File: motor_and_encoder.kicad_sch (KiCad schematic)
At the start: 6 parts, among them J5_1 Conn_02x03_Odd_Even, J5_2 Conn_02x03_Odd_Even, U5_1 DRV8835DSSR

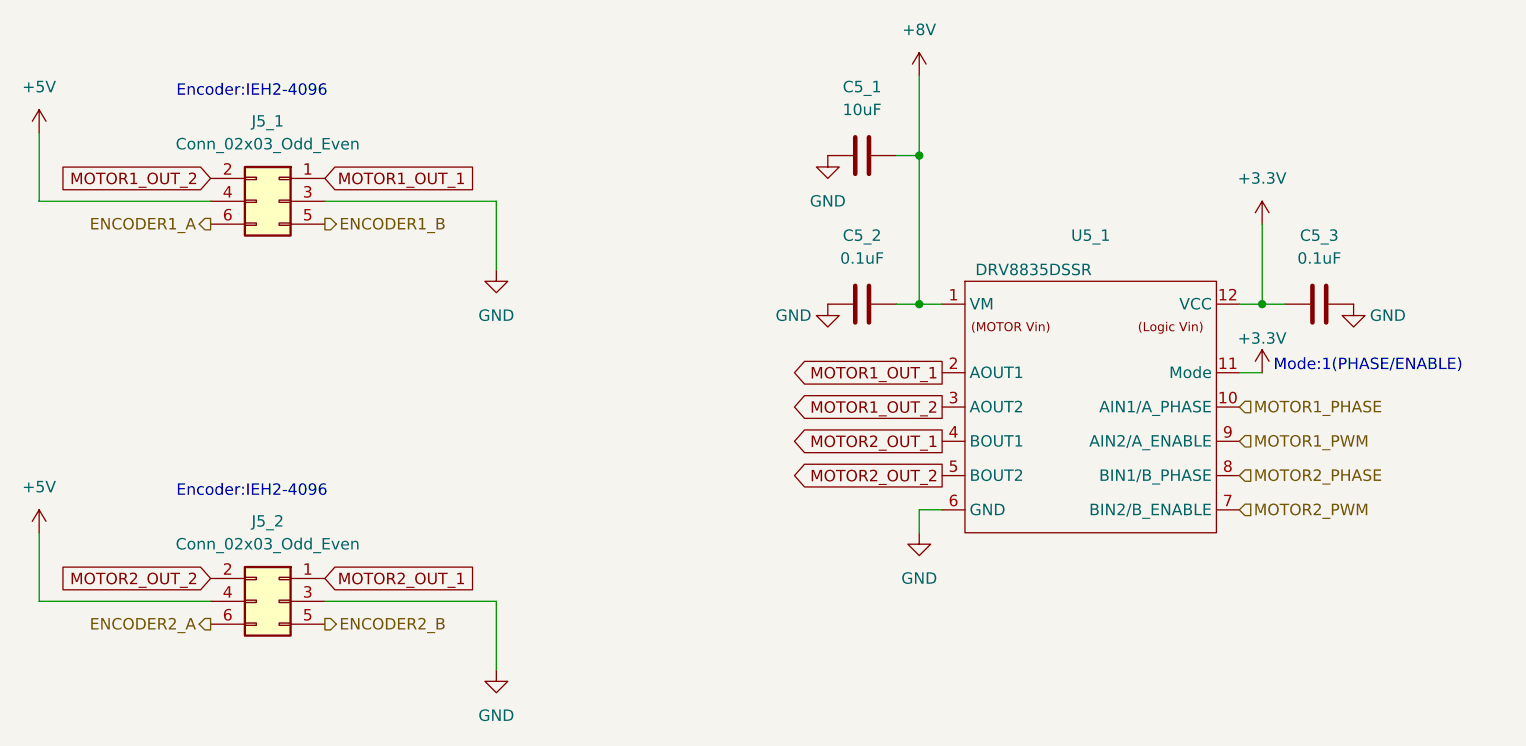
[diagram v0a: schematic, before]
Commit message: シンボルのモータの左右を入れ替え
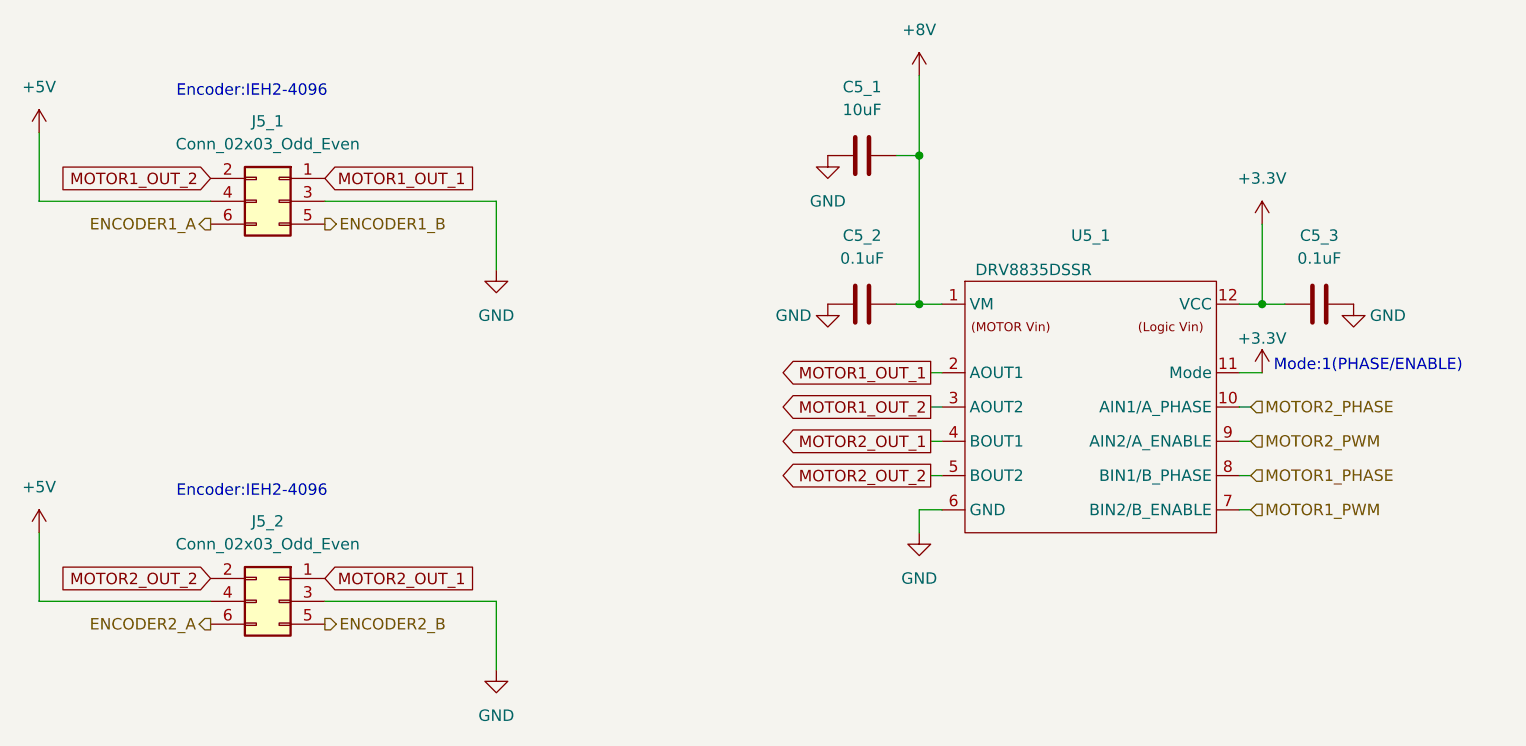
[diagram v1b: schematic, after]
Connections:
- net MOTOR1_PHASE: now also U5_1.8 (BIN1/B_PHASE); no longer U5_1.10 (AIN1/A_PHASE)
- net MOTOR1_PWM: now also U5_1.7 (BIN2/B_ENABLE); no longer U5_1.9 (AIN2/A_ENABLE)
- net MOTOR2_PHASE: now also U5_1.10 (AIN1/A_PHASE); no longer U5_1.8 (BIN1/B_PHASE)
- net MOTOR2_PWM: now also U5_1.9 (AIN2/A_ENABLE); no longer U5_1.7 (BIN2/B_ENABLE)
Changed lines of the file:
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@@
+    (stroke (width 0) (type default))
+  )
+  (wire (pts (xy 191.77 102.87) (xy 193.04 102.87))
     (stroke (width 0) (type default))
   )
   (wire (pts (xy 156.21 58.42) (xy 156.21 67.31))
+    (stroke (width 0) (type default))
+  )
+  (wire (pts (xy 191.77 95.25) (xy 193.04 95.25))
     (stroke (width 0) (type default))
   )
@@
     (stroke (width 0) (type default))
   )
+  (wire (pts (xy 157.48 95.25) (xy 158.75 95.25))
+    (stroke (width 0) (type default))
+  )
   (wire (pts (xy 109.22 72.39) (xy 90.17 72.39))
     (stroke (width 0) (type default))
   )
   (wire (pts (xy 153.67 83.82) (xy 156.21 83.82))
+    (stroke (width 0) (type default))
+  )
+  (wire (pts (xy 157.48 91.44) (xy 158.75 91.44))
     (stroke (width 0) (type default))
   )
@@
     (stroke (width 0) (type default))
   )
+  (wire (pts (xy 157.48 102.87) (xy 158.75 102.87))
+    (stroke (width 0) (type default))
+  )
+  (wire (pts (xy 191.77 106.68) (xy 193.04 106.68))
+    (stroke (width 0) (type default))
+  )
   (wire (pts (xy 109.22 72.39) (xy 109.22 80.01))
     (stroke (width 0) (type default))
   )
   (wire (pts (xy 109.22 116.84) (xy 109.22 124.46))
+    (stroke (width 0) (type default))
+  )
+  (wire (pts (xy 191.77 99.06) (xy 193.04 99.06))
+    (stroke (width 0) (type default))
+  )
+  (wire (pts (xy 157.48 99.06) (xy 158.75 99.06))
     (stroke (width 0) (type default))
   )
@@
     (effects (font (size 1.27 1.27)) (justify left bottom))
   )
-  (global_label "MOTOR1_OUT_2" (shape output) (at 158.75 95.25 180) (fields_autoplaced)
+  (global_label "MOTOR1_OUT_2" (shape output) (at 157.48 95.25 180) (fields_autoplaced)
     (effects (font (size 1.27 1.27)) (justify right))
-    (property "Intersheetrefs" "${INTERSHEET_REFS}" (at 141.432 95.25 0)
+    (property "Intersheetrefs" "${INTERSHEET_REFS}" (at 140.162 95.25 0)
       (effects (font (size 1.27 1.27)) (justify right) hide)
     )
   )
-  (global_label "MOTOR2_OUT_2" (shape output) (at 158.75 102.87 180) (fields_autoplaced)
+  (global_label "MOTOR2_OUT_2" (shape output) (at 157.48 102.87 180) (fields_autoplaced)
     (effects (font (size 1.27 1.27)) (justify right))
-    (property "Intersheetrefs" "${INTERSHEET_REFS}" (at 141.432 102.87 0)
+    (property "Intersheetrefs" "${INTERSHEET_REFS}" (at 140.162 102.87 0)
       (effects (font (size 1.27 1.27)) (justify right) hide)
     )
   )
-  (global_label "MOTOR1_OUT_1" (shape output) (at 158.75 91.44 180) (fields_autoplaced)
+  (global_label "MOTOR1_OUT_1" (shape output) (at 157.48 91.44 180) (fields_autoplaced)
     (effects (font (size 1.27 1.27)) (justify right))
-    (property "Intersheetrefs" "${INTERSHEET_REFS}" (at 141.432 91.44 0)
+    (property "Intersheetrefs" "${INTERSHEET_REFS}" (at 140.162 91.44 0)
       (effects (font (size 1.27 1.27)) (justify right) hide)
     )
   )
-  (global_label "MOTOR2_OUT_1" (shape output) (at 158.75 99.06 180) (fields_autoplaced)
+  (global_label "MOTOR2_OUT_1" (shape output) (at 157.48 99.06 180) (fields_autoplaced)
     (effects (font (size 1.27 1.27)) (justify right))
-    (property "Intersheetrefs" "${INTERSHEET_REFS}" (at 141.432 99.06 0)
+    (property "Intersheetrefs" "${INTERSHEET_REFS}" (at 140.162 99.06 0)
       (effects (font (size 1.27 1.27)) (justify right) hide)
     )
@@
     (effects (font (size 1.27 1.27)) (justify right))
   )
-  (hierarchical_label "MOTOR1_PWM" (shape input) (at 191.77 99.06 0) (fields_autoplaced)
+  (hierarchical_label "MOTOR1_PWM" (shape input) (at 193.04 106.68 0) (fields_autoplaced)
     (effects (font (size 1.27 1.27)) (justify left))
   )
-  (hierarchical_label "MOTOR2_PWM" (shape input) (at 191.77 106.68 0) (fields_autoplaced)
+  (hierarchical_label "MOTOR2_PWM" (shape input) (at 193.04 99.06 0) (fields_autoplaced)
     (effects (font (size 1.27 1.27)) (justify left))
   )
-  (hierarchical_label "MOTOR1_PHASE" (shape input) (at 191.77 95.25 0) (fields_autoplaced)
+  (hierarchical_label "MOTOR1_PHASE" (shape input) (at 193.04 102.87 0) (fields_autoplaced)
     (effects (font (size 1.27 1.27)) (justify left))
   )
-  (hierarchical_label "MOTOR2_PHASE" (shape input) (at 191.77 102.87 0) (fields_autoplaced)
+  (hierarchical_label "MOTOR2_PHASE" (shape input) (at 193.04 95.25 0) (fields_autoplaced)
     (effects (font (size 1.27 1.27)) (justify left))
   )

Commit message: モータの左右入れ替えをpcbにも反映
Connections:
- net MOTOR1_OUT_1: now also U5_1.4 (BOUT1); no longer U5_1.2 (AOUT1)
- net MOTOR1_OUT_2: now also U5_1.5 (BOUT2); no longer U5_1.3 (AOUT2)
- net MOTOR2_OUT_1: now also U5_1.2 (AOUT1); no longer U5_1.4 (BOUT1)
- net MOTOR2_OUT_2: now also U5_1.3 (AOUT2); no longer U5_1.5 (BOUT2)
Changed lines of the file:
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@@
+    (stroke (width 0) (type default))
+  )
+  (wire (pts (xy 157.48 91.44) (xy 158.75 91.44))
     (stroke (width 0) (type default))
   )
@@
     (stroke (width 0) (type default))
   )
+  (wire (pts (xy 157.48 99.06) (xy 158.75 99.06))
+    (stroke (width 0) (type default))
+  )
   (wire (pts (xy 157.48 95.25) (xy 158.75 95.25))
     (stroke (width 0) (type default))
@@
     (stroke (width 0) (type default))
   )
-  (wire (pts (xy 157.48 91.44) (xy 158.75 91.44))
+  (wire (pts (xy 58.42 116.84) (xy 77.47 116.84))
     (stroke (width 0) (type default))
   )
-  (wire (pts (xy 58.42 116.84) (xy 77.47 116.84))
+  (wire (pts (xy 157.48 102.87) (xy 158.75 102.87))
     (stroke (width 0) (type default))
   )
@@
   )
   (wire (pts (xy 196.85 83.82) (xy 194.31 83.82))
-    (stroke (width 0) (type default))
-  )
-  (wire (pts (xy 157.48 102.87) (xy 158.75 102.87))
     (stroke (width 0) (type default))
   )
@@
   )
   (wire (pts (xy 191.77 99.06) (xy 193.04 99.06))
-    (stroke (width 0) (type default))
-  )
-  (wire (pts (xy 157.48 99.06) (xy 158.75 99.06))
     (stroke (width 0) (type default))
   )
@@
     (effects (font (size 1.27 1.27)) (justify left bottom))
   )
-  (global_label "MOTOR1_OUT_2" (shape output) (at 157.48 95.25 180) (fields_autoplaced)
+  (global_label "MOTOR1_OUT_2" (shape output) (at 157.48 102.87 180) (fields_autoplaced)
+    (effects (font (size 1.27 1.27)) (justify right))
+    (property "Intersheetrefs" "${INTERSHEET_REFS}" (at 140.162 102.87 0)
+      (effects (font (size 1.27 1.27)) (justify right) hide)
+    )
+  )
+  (global_label "MOTOR2_OUT_2" (shape output) (at 157.48 95.25 180) (fields_autoplaced)
     (effects (font (size 1.27 1.27)) (justify right))
     (property "Intersheetrefs" "${INTERSHEET_REFS}" (at 140.162 95.25 0)
@@
     )
   )
-  (global_label "MOTOR2_OUT_2" (shape output) (at 157.48 102.87 180) (fields_autoplaced)
+  (global_label "MOTOR1_OUT_1" (shape output) (at 157.48 99.06 180) (fields_autoplaced)
     (effects (font (size 1.27 1.27)) (justify right))
-    (property "Intersheetrefs" "${INTERSHEET_REFS}" (at 140.162 102.87 0)
+    (property "Intersheetrefs" "${INTERSHEET_REFS}" (at 140.162 99.06 0)
       (effects (font (size 1.27 1.27)) (justify right) hide)
     )
   )
-  (global_label "MOTOR1_OUT_1" (shape output) (at 157.48 91.44 180) (fields_autoplaced)
+  (global_label "MOTOR2_OUT_1" (shape output) (at 157.48 91.44 180) (fields_autoplaced)
     (effects (font (size 1.27 1.27)) (justify right))
     (property "Intersheetrefs" "${INTERSHEET_REFS}" (at 140.162 91.44 0)
       (effects (font (size 1.27 1.27)) (justify right) hide)
     )
-  )
-  (global_label "MOTOR2_OUT_1" (shape output) (at 157.48 99.06 180) (fields_autoplaced)
-    (effects (font (size 1.27 1.27)) (justify right))
-    (property "Intersheetrefs" "${INTERSHEET_REFS}" (at 140.162 99.06 0)
-      (effects (font (size 1.27 1.27)) (justify right) hide)
-    )
